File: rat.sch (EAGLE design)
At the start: 66 parts, among them J1 B2B-PH-K-S(LF)(SN), J2 B2B-PH-K-S(LF)(SN), J3 PPTC041LFBN-RC, J4 PPTC081LFBN-RCCONN_PPTC081LFB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, Q1A SFH_313_FA-3/4, Q1B SFH_313_FA-3/4, Q1C SFH_313_FA-3/4, Q1D SFH_313_FA-3/4, Q2A Q2, Q2B Q2, Q2C Q2, Q2D Q2, U1 L293DD, U2 LD1117D33CTR, U3 STM32F205RGT6

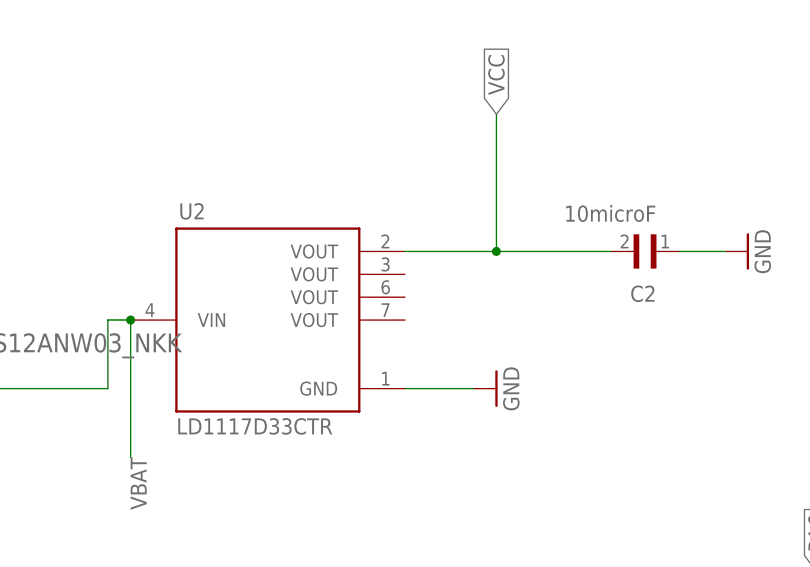
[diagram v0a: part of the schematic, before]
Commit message: First 6 Review-Required Changes Complete
Detailed in the "Team 27 PCB Review" Google Doc
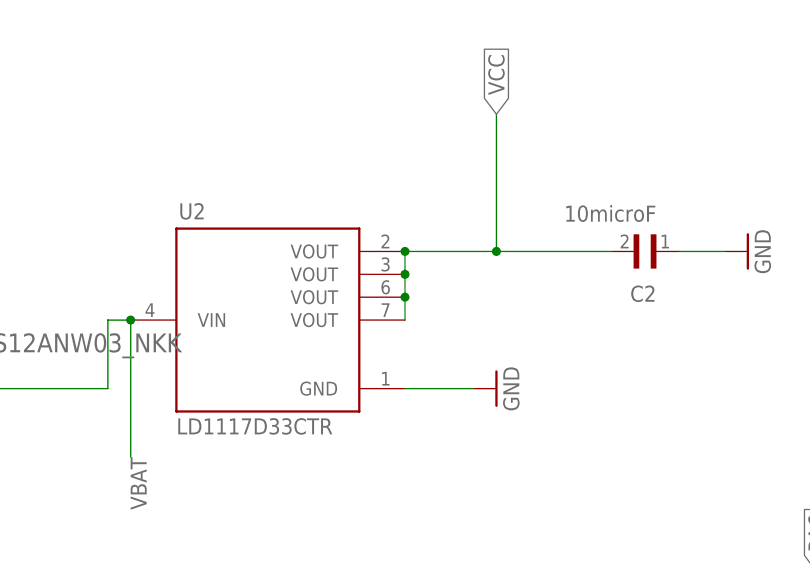
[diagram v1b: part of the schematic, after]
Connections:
- net VCC: now also U2.VOUT@2, U2.VOUT@3, U2.VOUT@4
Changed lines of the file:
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@@
 <wire x1="66.04" y1="-91.44" x2="66.04" y2="-76.2" width="0.1524" layer="91"/>
 <pinref part="C2" gate="G$1" pin="2"/>
+<pinref part="U2" gate="G$1" pin="VOUT@4"/>
+<wire x1="55.88" y1="-91.44" x2="55.88" y2="-93.98" width="0.1524" layer="91"/>
+<junction x="55.88" y="-91.44"/>
+<pinref part="U2" gate="G$1" pin="VOUT@2"/>
+<wire x1="55.88" y1="-93.98" x2="55.88" y2="-96.52" width="0.1524" layer="91"/>
+<junction x="55.88" y="-93.98"/>
+<pinref part="U2" gate="G$1" pin="VOUT@3"/>
+<wire x1="55.88" y1="-96.52" x2="55.88" y2="-99.06" width="0.1524" layer="91"/>
+<junction x="55.88" y="-96.52"/>
 </segment>
 </net>

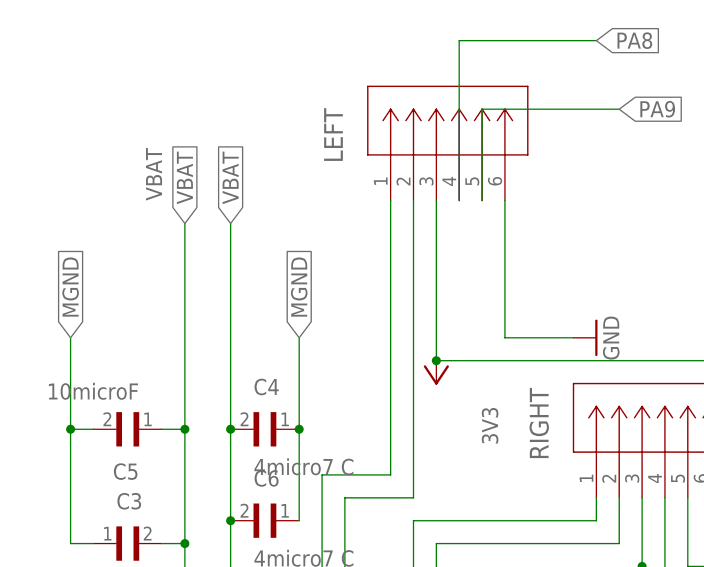
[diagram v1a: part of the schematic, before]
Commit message: Most of Crucial Changes Made
Still need to fix rest of trace sizes, make sure all decoupling capacitors are near the correct components, and switch out the incorrect MOSFET for the correct part.
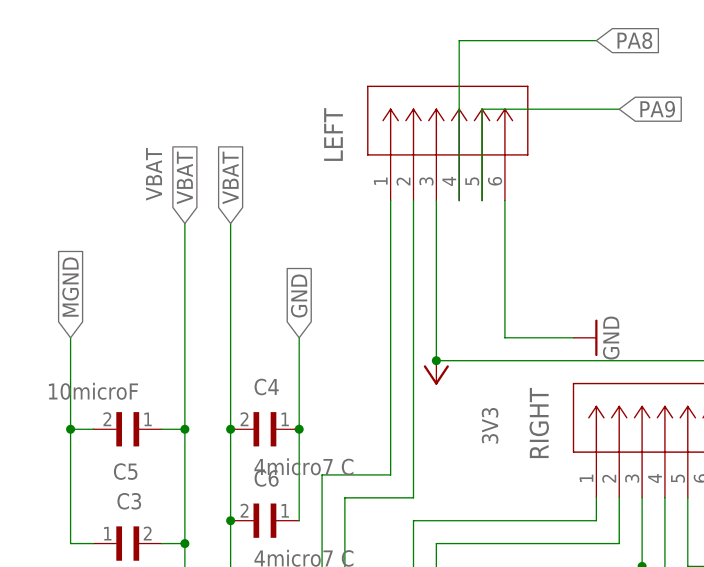
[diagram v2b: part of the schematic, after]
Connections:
- net GND: now also C4.1, C6.1
- net MGND: no longer C4.1, C6.1
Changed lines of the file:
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@@
 <attribute name="VALUE" x="-15.24" y="30.48" size="1.778" layer="96" rot="R90"/>
 </instance>
-<instance part="Q1A" gate="G$1" x="454.66" y="-50.8" smashed="yes" rot="R180" grouprefs="RECIEVERS RECEIVER_A">
+<instance part="Q1A" gate="G$1" x="454.66" y="-50.8" smashed="yes" rot="R180" grouprefs="RECEIVER_A RECIEVERS">
 <attribute name="NAME" x="464.8156" y="-55.8822" size="1.779540625" layer="95" rot="R180"/>
 <attribute name="VALUE" x="447.04" y="-45.7292" size="1.78121875" layer="96" rot="R270"/>
@@
 <pinref part="GND1" gate="1" pin="GND"/>
 <wire x1="55.88" y1="-106.68" x2="63.5" y2="-106.68" width="0.1524" layer="91"/>
+</segment>
+<segment>
+<wire x1="-71.12" y1="50.8" x2="-71.12" y2="40.64" width="0.1524" layer="91" grouprefs="MOTOR_AND_ENCODERS"/>
+<pinref part="C4" gate="G$1" pin="1"/>
+<wire x1="-71.12" y1="40.64" x2="-71.12" y2="30.48" width="0.1524" layer="91" grouprefs="MOTOR_AND_ENCODERS"/>
+<junction x="-71.12" y="40.64"/>
+<pinref part="C6" gate="G$1" pin="1"/>
+<label x="-71.12" y="50.8" size="1.778" layer="95" rot="R90" xref="yes"/>
 </segment>
 </net>
@@
 <segment>
 <pinref part="Q1A" gate="G$1" pin="E"/>
-<wire x1="452.12" y1="-45.72" x2="452.12" y2="-40.64" width="0.1524" layer="91" grouprefs="RECIEVERS RECEIVER_A"/>
-<wire x1="452.12" y1="-40.64" x2="449.58" y2="-40.64" width="0.1524" layer="91" grouprefs="RECIEVERS RECEIVER_A"/>
-<wire x1="452.12" y1="-40.64" x2="452.12" y2="-35.56" width="0.1524" layer="91" grouprefs="RECIEVERS RECEIVER_A"/>
-<junction x="452.12" y="-40.64" grouprefs="RECIEVERS RECEIVER_A"/>
+<wire x1="452.12" y1="-45.72" x2="452.12" y2="-40.64" width="0.1524" layer="91" grouprefs="RECEIVER_A RECIEVERS"/>
+<wire x1="452.12" y1="-40.64" x2="449.58" y2="-40.64" width="0.1524" layer="91" grouprefs="RECEIVER_A RECIEVERS"/>
+<wire x1="452.12" y1="-40.64" x2="452.12" y2="-35.56" width="0.1524" layer="91" grouprefs="RECEIVER_A RECIEVERS"/>
+<junction x="452.12" y="-40.64" grouprefs="RECEIVER_A RECIEVERS"/>
 <wire x1="449.58" y1="15.24" x2="449.58" y2="-40.64" width="0.1524" layer="91" grouprefs="RECIEVERS"/>
 <pinref part="R1A" gate="G$1" pin="1"/>
@@
 <label x="-50.8" y="22.86" size="1.778" layer="95"/>
 </segment>
-<segment>
-<wire x1="-71.12" y1="50.8" x2="-71.12" y2="40.64" width="0.1524" layer="91" grouprefs="MOTOR_AND_ENCODERS"/>
-<pinref part="C4" gate="G$1" pin="1"/>
-<wire x1="-71.12" y1="40.64" x2="-71.12" y2="30.48" width="0.1524" layer="91" grouprefs="MOTOR_AND_ENCODERS"/>
-<junction x="-71.12" y="40.64"/>
-<pinref part="C6" gate="G$1" pin="1"/>
-<label x="-71.12" y="50.8" size="1.778" layer="95" rot="R90" xref="yes"/>
-</segment>
-</net>
+</net>

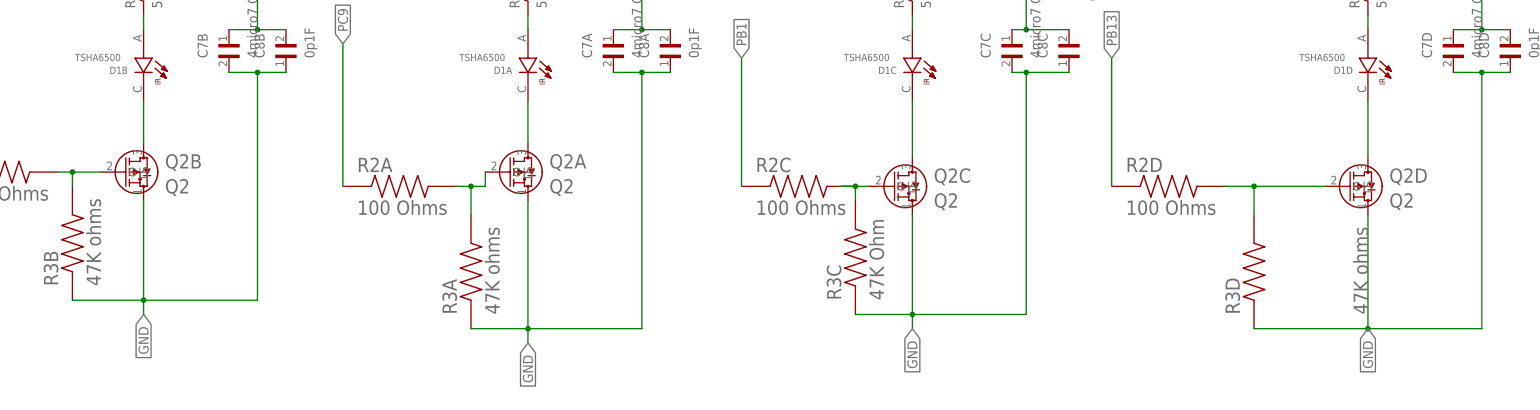
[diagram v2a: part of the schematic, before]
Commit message: DRC Cleared
Necessary changes: make sure decoupling capacitors are near components, adjust power trace sizes
Suggested Changes: clarify silkscreen, narrow board, round pcb corners
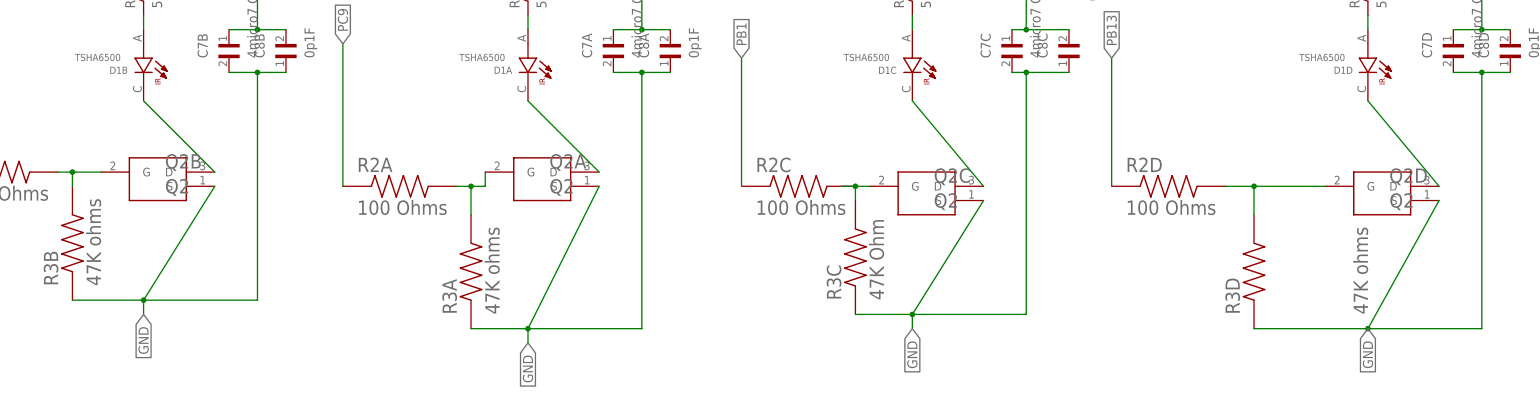
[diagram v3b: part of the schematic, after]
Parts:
- Q2A, Q2B, Q2C, Q2D: device 2022-01-23_01-58-16_Library:RZF020P01TLTRANS_RZF013P_ROM -> SamacSys_Parts:2N7000_D26Z
